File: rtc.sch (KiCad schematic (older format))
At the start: 9 parts

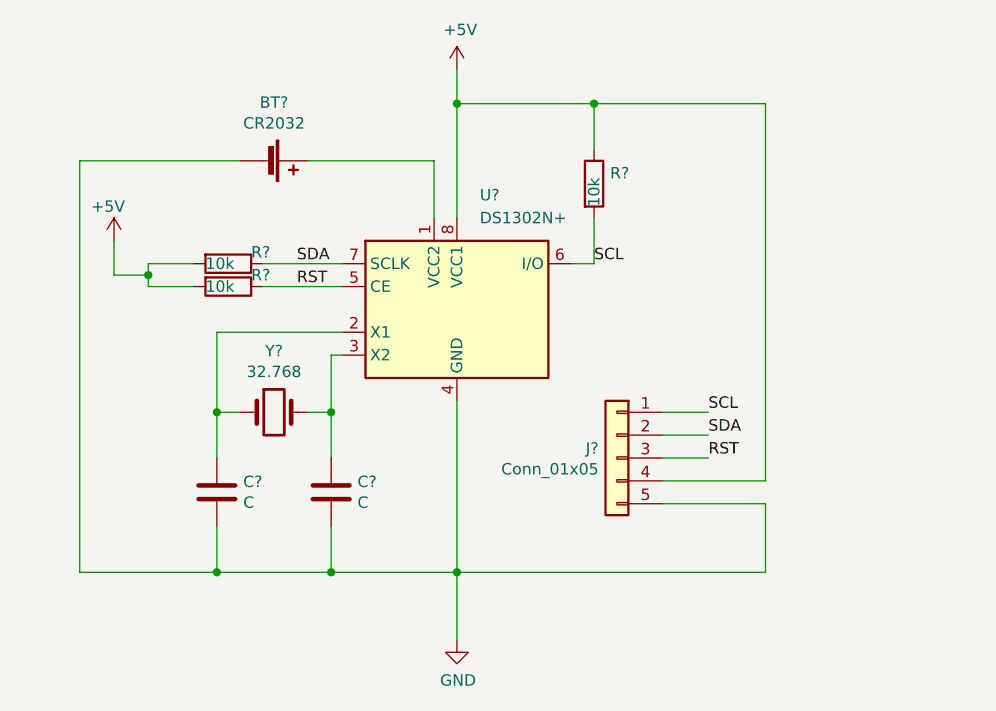
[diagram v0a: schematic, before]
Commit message: Tweak schematic and add pwr markers. Assign footprints.
- Generate net list
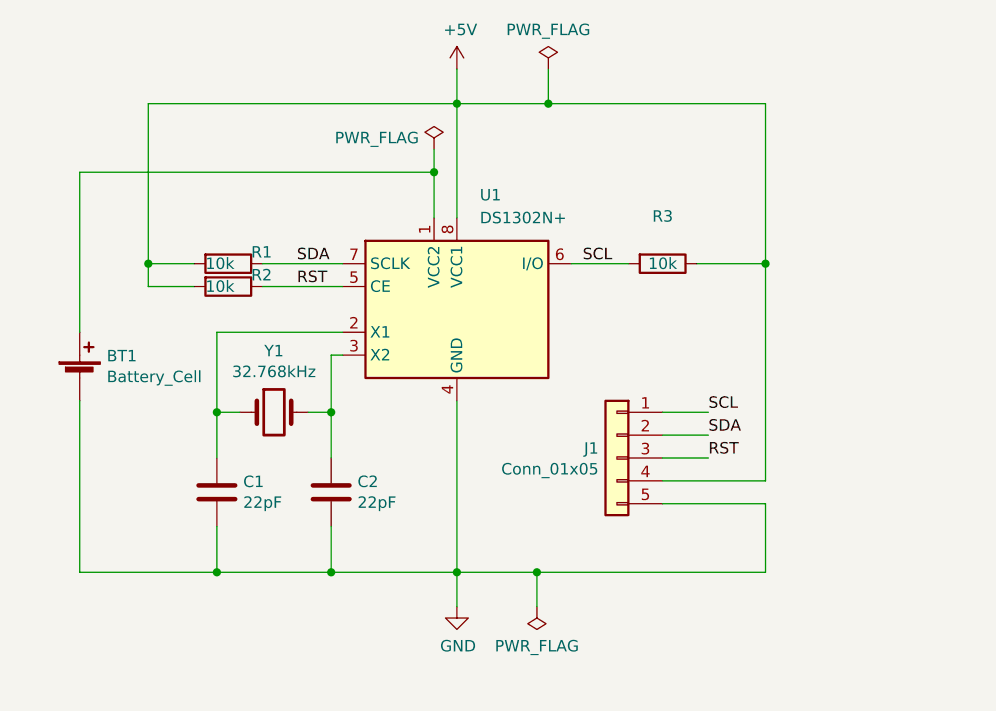
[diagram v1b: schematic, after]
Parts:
- removed BT?: CR2032, symbol Device:Battery_Cell
- removed R?: 10k, symbol Device:R
- added BT1: Battery_Cell, Battery:BatteryHolder_Keystone_1060_1x2032, symbol Device:Battery_Cell
- added R3: 10k, Resistor_SMD:R_1206_3216Metric_Pad1.42x1.75mm_HandSolder, symbol Device:R
- C1, C2: renamed from C?; value C -> 22pF; footprint (none) -> Capacitor_SMD:C_1206_3216Metric_Pad1.42x1.75mm_HandSolder
- J1: renamed from J?; footprint (none) -> Connector_PinHeader_2.54mm:PinHeader_1x05_P2.54mm_Vertical
- R1, R2: renamed from R?; footprint (none) -> Resistor_SMD:R_1206_3216Metric_Pad1.42x1.75mm_HandSolder
- Y1: renamed from Y?; value 32.768 -> 32.768kHz; footprint (none) -> Crystal:Resonator-2Pin_W8.0mm_H3.5mm
- gave numbers to parts that had none: 1
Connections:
- net +5V: now also R3.1
- net GND: now also BT1.2 (-)
- net SCL: now also R3.2
- net at U1.1 (VCC2): now also BT1.1 (+)
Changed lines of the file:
@@
 $EndDescr
 $Comp
-L Timer_RTC:DS1302N+ U?
+L Timer_RTC:DS1302N+ U1
 U 1 1 5D85BF93
 P 2500 2200
-F 0 "U?" H 2600 2700 50  0000 L CNN
+F 0 "U1" H 2600 2700 50  0000 L CNN
 F 1 "DS1302N+" H 2600 2600 50  0000 L CNN
 F 2 "Package_DIP:DIP-8_W7.62mm" H 2500 1700 50  0001 C CNN
@@
 $EndComp
 $Comp
-L Device:Crystal Y?
+L Device:Crystal Y1
 U 1 1 5D85EEF2
 P 1700 2650
-F 0 "Y?" H 1700 2918 50  0000 C CNN
-F 1 "32.768" H 1700 2827 50  0000 C CNN
-F 2 "" H 1700 2650 50  0001 C CNN
+F 0 "Y1" H 1700 2918 50  0000 C CNN
+F 1 "32.768kHz" H 1700 2827 50  0000 C CNN
+F 2 "Crystal:Resonator-2Pin_W8.0mm_H3.5mm" H 1700 2650 50  0001 C CNN
 F 3 "~" H 1700 2650 50  0001 C CNN
 	1    1700 2650
@@
 Wire Wire Line
 	2000 2300 1450 2300
-$Comp
-L Device:Battery_Cell BT?
-U 1 1 5D860FFA
-P 1650 1550
-F 0 "BT?" V 1395 1600 50  0000 C CNN
-F 1 "CR2032" V 1486 1600 50  0000 C CNN
-F 2 "" V 1650 1610 50  0001 C CNN
-F 3 "~" V 1650 1610 50  0001 C CNN
-	1    1650 1550
-	0    1    1    0
-$EndComp
 Wire Wire Line
 	1450 2300 1450 2650
@@
 	1850 2650 1950 2650
 $Comp
-L Device:C C?
+L Device:C C1
 U 1 1 5D866396
 P 1450 3000
-F 0 "C?" H 1565 3046 50  0000 L CNN
-F 1 "C" H 1565 2955 50  0000 L CNN
-F 2 "" H 1488 2850 50  0001 C CNN
+F 0 "C1" H 1565 3046 50  0000 L CNN
+F 1 "22pF" H 1565 2955 50  0000 L CNN
+F 2 "Capacitor_SMD:C_1206_3216Metric_Pad1.42x1.75mm_HandSolder" H 1488 2850 50  0001 C CNN
 F 3 "~" H 1450 3000 50  0001 C CNN
 	1    1450 3000
@@
 $EndComp
 $Comp
-L Device:C C?
+L Device:C C2
 U 1 1 5D867589
 P 1950 3000
-F 0 "C?" H 2065 3046 50  0000 L CNN
-F 1 "C" H 2065 2955 50  0000 L CNN
-F 2 "" H 1988 2850 50  0001 C CNN
+F 0 "C2" H 2065 3046 50  0000 L CNN
+F 1 "22pF" H 2065 2955 50  0000 L CNN
+F 2 "Capacitor_SMD:C_1206_3216Metric_Pad1.42x1.75mm_HandSolder" H 1988 2850 50  0001 C CNN
 F 3 "~" H 1950 3000 50  0001 C CNN
 	1    1950 3000
@@
 	2500 2600 2500 3350
 $Comp
-L power:GND #PWR?
+L power:GND #PWR02
 U 1 1 5D86A1B2
-P 2500 3650
-F 0 "#PWR?" H 2500 3400 50  0001 C CNN
-F 1 "GND" H 2505 3477 50  0000 C CNN
-F 2 "" H 2500 3650 50  0001 C CNN
-F 3 "" H 2500 3650 50  0001 C CNN
-	1    2500 3650
-	1    0    0    -1
-$EndComp
-Wire Wire Line
-	2500 3350 2500 3650
-$Comp
-L Connector_Generic:Conn_01x05 J?
+P 2500 3500
+F 0 "#PWR02" H 2500 3250 50  0001 C CNN
+F 1 "GND" H 2505 3327 50  0000 C CNN
+F 2 "" H 2500 3500 50  0001 C CNN
+F 3 "" H 2500 3500 50  0001 C CNN
+	1    2500 3500
+	1    0    0    -1
+$EndComp
+$Comp
+L Connector_Generic:Conn_01x05 J1
 U 1 1 5D86BE0F
 P 3200 2850
-F 0 "J?" H 3280 2892 50  0000 L CNN
+F 0 "J1" H 3280 2892 50  0000 L CNN
 F 1 "Conn_01x05" H 3280 2801 50  0000 L CNN
-F 2 "" H 3200 2850 50  0001 C CNN
+F 2 "Connector_PinHeader_2.54mm:PinHeader_1x05_P2.54mm_Vertical" H 3200 2850 50  0001 C CNN
 F 3 "~" H 3200 2850 50  0001 C CNN
 	1    3200 2850
 	-1   0    0    -1
 $EndComp
-Wire Wire Line
-	850  1550 850  3350
 Connection ~ 1450 3350
-Wire Wire Line
-	2400 1550 2400 1800
-Wire Wire Line
-	1850 1550 2400 1550
-$Comp
-L Device:R R?
-U 1 1 5D87848B
-P 3100 1650
-F 0 "R?" H 3170 1696 50  0000 L CNN
-F 1 "10k" V 3100 1550 50  0000 L CNN
-F 2 "" V 3030 1650 50  0001 C CNN
-F 3 "~" H 3100 1650 50  0001 C CNN
-	1    3100 1650
-	1    0    0    -1
-$EndComp
-$Comp
-L Device:R R?
-U 1 1 5D87A0D8
-P 1500 2000
-F 0 "R?" V 1450 2100 50  0000 L CNN
-F 1 "10k" V 1500 1900 50  0000 L CNN
-F 2 "" V 1430 2000 50  0001 C CNN
-F 3 "~" H 1500 2000 50  0001 C CNN
-	1    1500 2000
-	0    1    1    0
-$EndComp
-$Comp
-L Device:R R?
-U 1 1 5D87AFD2
-P 1500 2100
-F 0 "R?" V 1450 2200 50  0000 L CNN
-F 1 "10k" V 1500 2000 50  0000 L CNN
-F 2 "" V 1430 2100 50  0001 C CNN
-F 3 "~" H 1500 2100 50  0001 C CNN
-	1    1500 2100
-	0    1    1    0
-$EndComp
-$Comp
-L power:+5V #PWR?
+$Comp
+L power:+5V #PWR01
 U 1 1 5D874E7B
 P 2500 1150
-F 0 "#PWR?" H 2500 1000 50  0001 C CNN
+F 0 "#PWR01" H 2500 1000 50  0001 C CNN
 F 1 "+5V" H 2515 1323 50  0000 C CNN
 F 2 "" H 2500 1150 50  0001 C CNN
@@
 	1    0    0    -1
 $EndComp
-$Comp
-L power:+5V #PWR?
-U 1 1 5D87CD03
-P 1000 1900
-F 0 "#PWR?" H 1000 1750 50  0001 C CNN
-F 1 "+5V" H 900 2050 50  0000 L CNN
-F 2 "" H 1000 1900 50  0001 C CNN
-F 3 "" H 1000 1900 50  0001 C CNN
-	1    1000 1900
-	1    0    0    -1
-$EndComp
-Wire Wire Line
-	1150 2000 1350 2000
-Wire Wire Line
-	1150 2100 1350 2100
-Wire Wire Line
-	1150 2000 1150 2050
-Wire Wire Line
-	1000 1900 1000 2050
-Wire Wire Line
-	1000 2050 1150 2050
-Connection ~ 1150 2050
-Wire Wire Line
-	1150 2050 1150 2100
 Wire Wire Line
 	2500 1150 2500 1300
-Wire Wire Line
-	3000 2000 3100 2000
-Wire Wire Line
-	3100 2000 3100 1800
-Wire Wire Line
-	3100 1300 2500 1300
 Connection ~ 2500 1300
 Wire Wire Line
 	2500 1300 2500 1800
-Wire Wire Line
-	3100 1300 3100 1500
-Wire Wire Line
-	850  1550 1550 1550
 Wire Wire Line
 	850  3350 1450 3350
@@
 Text Label 1800 2000 0    50   ~ 0
 SDA
-Text Label 3100 2000 0    50   ~ 0
+Text Label 3050 2000 0    50   ~ 0
 SCL
 Text Label 1800 2100 0    50   ~ 0
@@
 RST
 Wire Wire Line
-	3850 2950 3850 1300
-Wire Wire Line
-	3850 1300 3100 1300
+	3850 2950 3850 2000
 Wire Wire Line
 	3400 2950 3850 2950
-Connection ~ 3100 1300
 Wire Wire Line
 	3850 3050 3850 3350
 Wire Wire Line
-	3850 3350 2500 3350
+	3850 3350 2850 3350
 Wire Wire Line
 	3400 3050 3850 3050
 Connection ~ 2500 3350
+Wire Wire Line
+	1150 1300 2500 1300
+Wire Wire Line
+	1150 1300 1150 2000
+Connection ~ 1150 2000
+Wire Wire Line
+	1150 2000 1150 2100
+Wire Wire Line
+	850  1600 2400 1600
+$Comp
+L Device:Battery_Cell BT1
+U 1 1 5D892343
+P 850 2500
+F 0 "BT1" H 968 2596 50  0000 L CNN
+F 1 "Battery_Cell" H 968 2505 50  0000 L CNN
+F 2 "Battery:BatteryHolder_Keystone_1060_1x2032" V 850 2560 50  0001 C CNN
+F 3 "~" V 850 2560 50  0001 C CNN
+	1    850  2500
+	1    0    0    -1
+$EndComp
+Wire Wire Line
+	850  3350 850  2600
+Wire Wire Line
+	850  2300 850  1600
+Wire Wire Line
+	3000 2000 3250 2000
+Wire Wire Line
+	1150 2100 1350 2100
+Wire Wire Line
+	1150 2000 1350 2000
+$Comp
+L Device:R R2
+U 1 1 5D87AFD2
+P 1500 2100
+F 0 "R2" V 1450 2200 50  0000 L CNN
+F 1 "10k" V 1500 2000 50  0000 L CNN
+F 2 "Resistor_SMD:R_1206_3216Metric_Pad1.42x1.75mm_HandSolder" V 1430 2100 50  0001 C CNN
+F 3 "~" H 1500 2100 50  0001 C CNN
+	1    1500 2100
+	0    1    1    0
+$EndComp
+$Comp
+L Device:R R1
+U 1 1 5D87A0D8
+P 1500 2000
+F 0 "R1" V 1450 2100 50  0000 L CNN
+F 1 "10k" V 1500 1900 50  0000 L CNN
+F 2 "Resistor_SMD:R_1206_3216Metric_Pad1.42x1.75mm_HandSolder" V 1430 2000 50  0001 C CNN
+F 3 "~" H 1500 2000 50  0001 C CNN
+	1    1500 2000
+	0    1    1    0
+$EndComp
+Wire Wire Line
+	2500 1300 2900 1300
+$Comp
+L Device:R R3
+U 1 1 5D897C40
+P 3400 2000
+F 0 "R3" V 3193 2000 50  0000 C CNN
+F 1 "10k" V 3400 2000 50  0000 C CNN
+F 2 "Resistor_SMD:R_1206_3216Metric_Pad1.42x1.75mm_HandSolder" V 3330 2000 50  0001 C CNN
+F 3 "~" H 3400 2000 50  0001 C CNN
+	1    3400 2000
+	0    1    1    0
+$EndComp
+Wire Wire Line
+	3550 2000 3850 2000
+Connection ~ 3850 2000
+Wire Wire Line
+	3850 2000 3850 1300
+$Comp
+L power:PWR_FLAG #FLG0101
+U 1 1 5D89B8AC
+P 2900 1150
+F 0 "#FLG0101" H 2900 1225 50  0001 C CNN
+F 1 "PWR_FLAG" H 2900 1323 50  0000 C CNN
+F 2 "" H 2900 1150 50  0001 C CNN
+F 3 "~" H 2900 1150 50  0001 C CNN
+	1    2900 1150
+	1    0    0    -1
+$EndComp
+Wire Wire Line
+	2900 1150 2900 1300
+Connection ~ 2900 1300
+Wire Wire Line
+	2900 1300 3850 1300
+$Comp
+L power:PWR_FLAG #FLG0102
+U 1 1 5D89F02D
+P 2850 3500
+F 0 "#FLG0102" H 2850 3575 50  0001 C CNN
+F 1 "PWR_FLAG" H 2850 3673 50  0000 C CNN
+F 2 "" H 2850 3500 50  0001 C CNN
+F 3 "~" H 2850 3500 50  0001 C CNN
+	1    2850 3500
+	-1   0    0    1
+$EndComp
+Wire Wire Line
+	2850 3500 2850 3350
+Connection ~ 2850 3350
+Wire Wire Line
+	2850 3350 2500 3350
+Wire Wire Line
+	2500 3500 2500 3350
+$Comp
+L power:PWR_FLAG #FLG0103
+U 1 1 5D8A4FC6
+P 2400 1500
+F 0 "#FLG0103" H 2400 1575 50  0001 C CNN
+F 1 "PWR_FLAG" H 2150 1550 50  0000 C CNN
+F 2 "" H 2400 1500 50  0001 C CNN
+F 3 "~" H 2400 1500 50  0001 C CNN
+	1    2400 1500
+	1    0    0    -1
+$EndComp
+Wire Wire Line
+	2400 1500 2400 1600
+Connection ~ 2400 1600
+Wire Wire Line
+	2400 1600 2400 1800
 $EndSCHEMATC

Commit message: Initial pcb layout and routing. Add readme/imgs.
- Added design rules for oshpark
- Added mounting holes and 30x50mm board outline
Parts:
- Y1: footprint Crystal:Resonator-2Pin_W8.0mm_H3.5mm -> Crystal:Crystal_HC49-U_Vertical
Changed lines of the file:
@@
 F 0 "Y1" H 1700 2918 50  0000 C CNN
 F 1 "32.768kHz" H 1700 2827 50  0000 C CNN
-F 2 "Crystal:Resonator-2Pin_W8.0mm_H3.5mm" H 1700 2650 50  0001 C CNN
+F 2 "Crystal:Crystal_HC49-U_Vertical" H 1700 2650 50  0001 C CNN
 F 3 "~" H 1700 2650 50  0001 C CNN
 	1    1700 2650

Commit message: Remove redundant pull-ups per datasheet
- Capacitors accross crystal removed per datasheet info on oscillator circuit
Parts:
- removed C1, C2: 22pF, Capacitor_SMD:C_1206_3216Metric_Pad1.42x1.75mm_HandSolder, symbol Device:C
- removed R1, R2, R3: 10k, Resistor_SMD:R_1206_3216Metric_Pad1.42x1.75mm_HandSolder, symbol Device:R
- added C3: 1uF, Capacitor_SMD:C_1206_3216Metric_Pad1.42x1.75mm_HandSolder, symbol rtc-rescue:C-Device
- BT1: symbol Device:Battery_Cell -> rtc-rescue:Battery_Cell-Device
- J1: symbol Connector_Generic:Conn_01x05 -> rtc-rescue:Conn_01x05-Connector_Generic
- U1: symbol Timer_RTC:DS1302N+ -> rtc-rescue:DS1302N+-Timer_RTC
- Y1: symbol Device:Crystal -> rtc-rescue:Crystal-Device
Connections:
- net labels added: CE, DAT, SCLK
- net labels removed: RST, SCL, SDA
- wire segments 45 -> 40
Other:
- moved on the sheet: Y1
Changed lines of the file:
@@
 EESchema Schematic File Version 4
+LIBS:rtc-cache
 EELAYER 29 0
 EELAYER END
@@
 $EndDescr
 $Comp
-L Timer_RTC:DS1302N+ U1
+L rtc-rescue:DS1302N+-Timer_RTC U1
 U 1 1 5D85BF93
 P 2500 2200
@@
 $EndComp
 $Comp
-L Device:Crystal Y1
+L rtc-rescue:Crystal-Device Y1
 U 1 1 5D85EEF2
-P 1700 2650
-F 0 "Y1" H 1700 2918 50  0000 C CNN
-F 1 "32.768kHz" H 1700 2827 50  0000 C CNN
-F 2 "Crystal:Crystal_HC49-U_Vertical" H 1700 2650 50  0001 C CNN
-F 3 "~" H 1700 2650 50  0001 C CNN
-	1    1700 2650
+P 1700 2850
+F 0 "Y1" H 1700 3118 50  0000 C CNN
+F 1 "32.768kHz" H 1700 3027 50  0000 C CNN
+F 2 "Crystal:Crystal_HC49-U_Vertical" H 1700 2850 50  0001 C CNN
+F 3 "~" H 1700 2850 50  0001 C CNN
+	1    1700 2850
 	1    0    0    -1
 $EndComp
@@
 	2000 2300 1450 2300
 Wire Wire Line
-	1450 2300 1450 2650
-Wire Wire Line
-	1550 2650 1450 2650
+	1550 2850 1450 2850
 Wire Wire Line
 	1950 2400 2000 2400
 Wire Wire Line
-	1950 2400 1950 2650
-Wire Wire Line
-	1850 2650 1950 2650
-$Comp
-L Device:C C1
-U 1 1 5D866396
-P 1450 3000
-F 0 "C1" H 1565 3046 50  0000 L CNN
-F 1 "22pF" H 1565 2955 50  0000 L CNN
-F 2 "Capacitor_SMD:C_1206_3216Metric_Pad1.42x1.75mm_HandSolder" H 1488 2850 50  0001 C CNN
-F 3 "~" H 1450 3000 50  0001 C CNN
-	1    1450 3000
-	1    0    0    -1
-$EndComp
-$Comp
-L Device:C C2
-U 1 1 5D867589
-P 1950 3000
-F 0 "C2" H 2065 3046 50  0000 L CNN
-F 1 "22pF" H 2065 2955 50  0000 L CNN
-F 2 "Capacitor_SMD:C_1206_3216Metric_Pad1.42x1.75mm_HandSolder" H 1988 2850 50  0001 C CNN
-F 3 "~" H 1950 3000 50  0001 C CNN
-	1    1950 3000
-	1    0    0    -1
-$EndComp
+	1850 2850 1950 2850
 Wire Wire Line
 	1450 3350 1950 3350
-Wire Wire Line
-	1450 2650 1450 2850
-Connection ~ 1450 2650
-Wire Wire Line
-	1450 3150 1450 3350
-Wire Wire Line
-	1950 3150 1950 3350
 Connection ~ 1950 3350
 Wire Wire Line
 	1950 3350 2500 3350
 Wire Wire Line
-	1950 2850 1950 2650
-Connection ~ 1950 2650
-Wire Wire Line
 	2500 2600 2500 3350
 $Comp
-L power:GND #PWR02
+L rtc-rescue:GND-power #PWR02
 U 1 1 5D86A1B2
 P 2500 3500
 F 0 "#PWR02" H 2500 3250 50  0001 C CNN
-F 1 "GND" H 2505 3327 50  0000 C CNN
+F 1 "GND" H 2500 3350 50  0000 C CNN
 F 2 "" H 2500 3500 50  0001 C CNN
 F 3 "" H 2500 3500 50  0001 C CNN
@@
 $EndComp
 $Comp
-L Connector_Generic:Conn_01x05 J1
+L rtc-rescue:Conn_01x05-Connector_Generic J1
 U 1 1 5D86BE0F
 P 3200 2850
@@
 $EndComp
 Connection ~ 1450 3350
-$Comp
-L power:+5V #PWR01
-U 1 1 5D874E7B
-P 2500 1150
-F 0 "#PWR01" H 2500 1000 50  0001 C CNN
-F 1 "+5V" H 2515 1323 50  0000 C CNN
-F 2 "" H 2500 1150 50  0001 C CNN
-F 3 "" H 2500 1150 50  0001 C CNN
-	1    2500 1150
-	1    0    0    -1
-$EndComp
-Wire Wire Line
-	2500 1150 2500 1300
-Connection ~ 2500 1300
-Wire Wire Line
-	2500 1300 2500 1800
 Wire Wire Line
 	850  3350 1450 3350
@@
 	1650 2100 2000 2100
 Text Label 1800 2000 0    50   ~ 0
-SDA
+SCLK
 Text Label 3050 2000 0    50   ~ 0
-SCL
+DAT
 Text Label 1800 2100 0    50   ~ 0
-RST
+CE
 Wire Wire Line
 	3400 2650 3600 2650
@@
 	3400 2850 3600 2850
 Text Label 3600 2650 0    50   ~ 0
-SCL
+SCLK
 Text Label 3600 2750 0    50   ~ 0
-SDA
+DAT
 Text Label 3600 2850 0    50   ~ 0
-RST
-Wire Wire Line
-	3850 2950 3850 2000
+CE
 Wire Wire Line
 	3400 2950 3850 2950
 Wire Wire Line
 	3850 3050 3850 3350
-Wire Wire Line
-	3850 3350 2850 3350
 Wire Wire Line
 	3400 3050 3850 3050
 Connection ~ 2500 3350
-Wire Wire Line
-	1150 1300 2500 1300
-Wire Wire Line
-	1150 1300 1150 2000
-Connection ~ 1150 2000
-Wire Wire Line
-	1150 2000 1150 2100
-Wire Wire Line
-	850  1600 2400 1600
-$Comp
-L Device:Battery_Cell BT1
+$Comp
+L rtc-rescue:Battery_Cell-Device BT1
 U 1 1 5D892343
 P 850 2500
@@
 	850  3350 850  2600
 Wire Wire Line
-	850  2300 850  1600
-Wire Wire Line
 	3000 2000 3250 2000
-Wire Wire Line
-	1150 2100 1350 2100
-Wire Wire Line
-	1150 2000 1350 2000
-$Comp
-L Device:R R2
-U 1 1 5D87AFD2
-P 1500 2100
-F 0 "R2" V 1450 2200 50  0000 L CNN
-F 1 "10k" V 1500 2000 50  0000 L CNN
-F 2 "Resistor_SMD:R_1206_3216Metric_Pad1.42x1.75mm_HandSolder" V 1430 2100 50  0001 C CNN
-F 3 "~" H 1500 2100 50  0001 C CNN
-	1    1500 2100
-	0    1    1    0
-$EndComp
-$Comp
-L Device:R R1
-U 1 1 5D87A0D8
-P 1500 2000
-F 0 "R1" V 1450 2100 50  0000 L CNN
-F 1 "10k" V 1500 1900 50  0000 L CNN
-F 2 "Resistor_SMD:R_1206_3216Metric_Pad1.42x1.75mm_HandSolder" V 1430 2000 50  0001 C CNN
-F 3 "~" H 1500 2000 50  0001 C CNN
-	1    1500 2000
-	0    1    1    0
-$EndComp
-Wire Wire Line
-	2500 1300 2900 1300
-$Comp
-L Device:R R3
-U 1 1 5D897C40
-P 3400 2000
-F 0 "R3" V 3193 2000 50  0000 C CNN
-F 1 "10k" V 3400 2000 50  0000 C CNN
-F 2 "Resistor_SMD:R_1206_3216Metric_Pad1.42x1.75mm_HandSolder" V 3330 2000 50  0001 C CNN
-F 3 "~" H 3400 2000 50  0001 C CNN
-	1    3400 2000
-	0    1    1    0
-$EndComp
-Wire Wire Line
-	3550 2000 3850 2000
-Connection ~ 3850 2000
-Wire Wire Line
-	3850 2000 3850 1300
-$Comp
-L power:PWR_FLAG #FLG0101
+$Comp
+L rtc-rescue:PWR_FLAG-power #FLG0102
+U 1 1 5D89F02D
+P 3000 3500
+F 0 "#FLG0102" H 3000 3575 50  0001 C CNN
+F 1 "PWR_FLAG" H 3000 3650 50  0000 C CNN
+F 2 "" H 3000 3500 50  0001 C CNN
+F 3 "~" H 3000 3500 50  0001 C CNN
+	1    3000 3500
+	-1   0    0    1
+$EndComp
+Wire Wire Line
+	3000 3500 3000 3350
+Wire Wire Line
+	2500 3500 2500 3350
+$Comp
+L rtc-rescue:C-Device C3
+U 1 1 5D8CE867
+P 4500 2500
+F 0 "C3" H 4615 2546 50  0000 L CNN
+F 1 "1uF" H 4615 2455 50  0000 L CNN
+F 2 "Capacitor_SMD:C_1206_3216Metric_Pad1.42x1.75mm_HandSolder" H 4538 2350 50  0001 C CNN
+F 3 "~" H 4500 2500 50  0001 C CNN
+	1    4500 2500
+	1    0    0    -1
+$EndComp
+Wire Wire Line
+	2500 1800 2500 1700
+Wire Wire Line
+	850  1700 850  2300
+Wire Wire Line
+	3850 1500 3850 2950
+Wire Wire Line
+	2400 1500 2400 1800
+Wire Wire Line
+	2400 1350 2400 1500
+$Comp
+L rtc-rescue:+5V-power #PWR01
+U 1 1 5D874E7B
+P 2400 1350
+F 0 "#PWR01" H 2400 1200 50  0001 C CNN
+F 1 "+5V" H 2400 1500 50  0000 C CNN
+F 2 "" H 2400 1350 50  0001 C CNN
+F 3 "" H 2400 1350 50  0001 C CNN
+	1    2400 1350
+	1    0    0    -1
+$EndComp
+Wire Wire Line
+	4500 3350 3850 3350
+Wire Wire Line
+	4500 2650 4500 3350
+Connection ~ 3850 3350
+Wire Wire Line
+	4500 1500 3850 1500
+Wire Wire Line
+	4500 1500 4500 2350
+Connection ~ 3850 1500
+Connection ~ 3000 3350
+Wire Wire Line
+	3000 3350 3850 3350
+Wire Wire Line
+	2500 3350 3000 3350
+Connection ~ 2400 1500
+Connection ~ 1450 2850
+Wire Wire Line
+	1450 2850 1450 3350
+Connection ~ 1950 2850
+Wire Wire Line
+	1950 2850 1950 3350
+Wire Wire Line
+	1450 2300 1450 2850
+Wire Wire Line
+	1950 2400 1950 2850
+Connection ~ 2800 1500
+Wire Wire Line
+	2400 1500 2800 1500
+Wire Wire Line
+	2800 1500 3850 1500
+$Comp
+L rtc-rescue:PWR_FLAG-power #FLG0101
 U 1 1 5D89B8AC
-P 2900 1150
-F 0 "#FLG0101" H 2900 1225 50  0001 C CNN
-F 1 "PWR_FLAG" H 2900 1323 50  0000 C CNN
-F 2 "" H 2900 1150 50  0001 C CNN
-F 3 "~" H 2900 1150 50  0001 C CNN
-	1    2900 1150
-	1    0    0    -1
-$EndComp
-Wire Wire Line
-	2900 1150 2900 1300
-Connection ~ 2900 1300
-Wire Wire Line
-	2900 1300 3850 1300
-$Comp
-L power:PWR_FLAG #FLG0102
-U 1 1 5D89F02D
-P 2850 3500
-F 0 "#FLG0102" H 2850 3575 50  0001 C CNN
-F 1 "PWR_FLAG" H 2850 3673 50  0000 C CNN
-F 2 "" H 2850 3500 50  0001 C CNN
-F 3 "~" H 2850 3500 50  0001 C CNN
-	1    2850 3500
-	-1   0    0    1
-$EndComp
-Wire Wire Line
-	2850 3500 2850 3350
-Connection ~ 2850 3350
-Wire Wire Line
-	2850 3350 2500 3350
-Wire Wire Line
-	2500 3500 2500 3350
-$Comp
-L power:PWR_FLAG #FLG0103
+P 2800 1350
+F 0 "#FLG0101" H 2800 1425 50  0001 C CNN
+F 1 "PWR_FLAG" H 2800 1523 50  0000 C CNN
+F 2 "" H 2800 1350 50  0001 C CNN
+F 3 "~" H 2800 1350 50  0001 C CNN
+	1    2800 1350
+	1    0    0    -1
+$EndComp
+Wire Wire Line
+	2800 1350 2800 1500
+Connection ~ 850  1700
+Wire Wire Line
+	2500 1700 850  1700
+Wire Wire Line
+	850  1500 850  1700
+$Comp
+L rtc-rescue:PWR_FLAG-power #FLG0103
 U 1 1 5D8A4FC6
-P 2400 1500
-F 0 "#FLG0103" H 2400 1575 50  0001 C CNN
-F 1 "PWR_FLAG" H 2150 1550 50  0000 C CNN
-F 2 "" H 2400 1500 50  0001 C CNN
-F 3 "~" H 2400 1500 50  0001 C CNN
-	1    2400 1500
-	1    0    0    -1
-$EndComp
-Wire Wire Line
-	2400 1500 2400 1600
-Connection ~ 2400 1600
-Wire Wire Line
-	2400 1600 2400 1800
+P 850 1500
+F 0 "#FLG0103" H 850 1575 50  0001 C CNN
+F 1 "PWR_FLAG" H 850 1700 50  0000 C CNN
+F 2 "" H 850 1500 50  0001 C CNN
+F 3 "~" H 850 1500 50  0001 C CNN
+	1    850  1500
+	1    0    0    -1
+$EndComp
 $EndSCHEMATC
